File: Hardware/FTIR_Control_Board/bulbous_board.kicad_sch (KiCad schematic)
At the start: 26 parts, among them J1 RJ45_LED_Shielded, Q1 NMOS, U1 OKI, U2 Peensy4.1_DEV-16771, U3 TMC2208

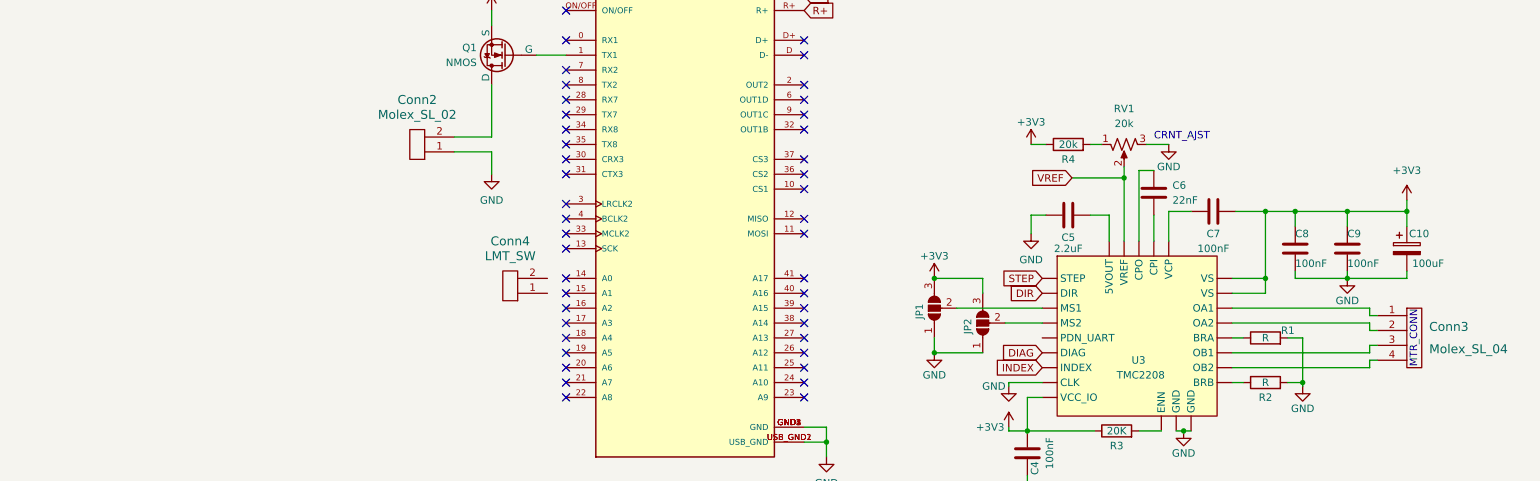
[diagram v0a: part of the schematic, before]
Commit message: Added Photodetector
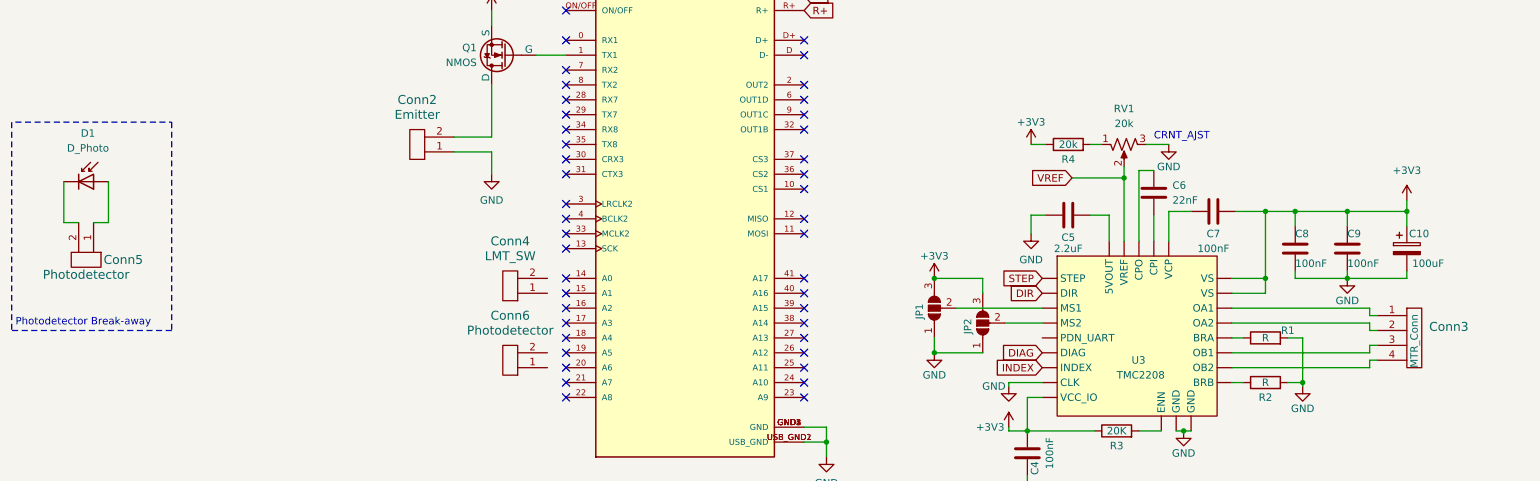
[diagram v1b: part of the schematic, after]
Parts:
- added Conn5, Conn6: Photodetector, symbol MRDT_Connectors:Molex_SL_02
- added D1: D_Photo, symbol Device:D_Photo
- Conn2: value Molex_SL_02 -> Emitter
- Conn3: value Molex_SL_04 -> MTR_Conn
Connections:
- new net: Conn5.2, D1.1 (K)
- new net: Conn5.1, D1.2 (A)
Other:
- note added: "Photodetector Break-away"
- note removed: "MTR_CONN"
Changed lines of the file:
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@@
     (stroke (width 0) (type default))
+  )
+  (polyline (pts (xy 24.13 93.345) (xy 24.13 128.905))
+    (stroke (width 0) (type dash))
   )
   (wire (pts (xy 238.125 108.585) (xy 238.125 120.015))
@@
     (stroke (width 0) (type default))
   )
+  (wire (pts (xy 38.1 110.49) (xy 40.64 110.49))
+    (stroke (width 0) (type default))
+  )
   (wire (pts (xy 163.195 147.955) (xy 163.195 150.495))
     (stroke (width 0) (type default))
@@
     (stroke (width 0) (type default))
   )
+  (wire (pts (xy 35.56 110.49) (xy 33.02 110.49))
+    (stroke (width 0) (type default))
+  )
   (wire (pts (xy 262.255 118.745) (xy 262.255 120.015))
     (stroke (width 0) (type default))
@@
     (stroke (width 0) (type default))
   )
+  (wire (pts (xy 33.02 110.49) (xy 33.02 103.505))
+    (stroke (width 0) (type default))
+  )
   (wire (pts (xy 79.375 33.02) (xy 83.185 33.02))
     (stroke (width 0) (type default))
@@
     (stroke (width 0) (type default))
   )
+  (polyline (pts (xy 51.435 93.345) (xy 51.435 128.905))
+    (stroke (width 0) (type dash))
+  )
   (wire (pts (xy 255.905 131.445) (xy 257.175 131.445))
     (stroke (width 0) (type default))
@@
     (stroke (width 0) (type default))
   )
+  (polyline (pts (xy 24.765 93.345) (xy 51.435 93.345))
+    (stroke (width 0) (type dash))
+  )
   (wire (pts (xy 271.145 53.975) (xy 274.955 53.975))
     (stroke (width 0) (type default))
@@
     (stroke (width 0) (type default))
   )
+  (wire (pts (xy 40.64 110.49) (xy 40.64 103.505))
+    (stroke (width 0) (type default))
+  )
   (wire (pts (xy 241.935 130.175) (xy 244.475 130.175))
     (stroke (width 0) (type default))
@@
   (wire (pts (xy 274.955 22.225) (xy 274.955 53.975))
     (stroke (width 0) (type default))
+  )
+  (polyline (pts (xy 51.435 128.905) (xy 24.13 128.905))
+    (stroke (width 0) (type dash))
   )
   (wire (pts (xy 193.675 127.635) (xy 200.025 127.635))
@@
     (effects (font (size 1.27 1.27)) (justify left bottom))
   )
-  (text "MTR_CONN" (at 264.16 135.255 90)
+  (text "Photodetector Break-away" (at 24.765 128.27 0)
     (effects (font (size 1.27 1.27)) (justify left bottom))
   )
@@
     )
   )
+  (symbol (lib_id "Device:D_Photo") (at 38.1 103.505 0) (unit 1)
+    (in_bom yes) (on_board yes) (dnp no) (fields_autoplaced)
+    (property "Reference" "D1" (at 37.1475 95.25 0)
+      (effects (font (size 1.27 1.27)))
+    )
+    (property "Value" "D_Photo" (at 37.1475 97.79 0)
+      (effects (font (size 1.27 1.27)))
+    )
+    (property "Footprint" "" (at 36.83 103.505 0)
+      (effects (font (size 1.27 1.27)) hide)
+    )
+    (property "Datasheet" "~" (at 36.83 103.505 0)
+      (effects (font (size 1.27 1.27)) hide)
+    )
+    (pin "1")
+    (pin "2")
+    (instances
+      (project "bulbous_board"
+        (path "/049c3f09-c046-40c3-9872-e62b40667976"
+          (reference "D1") (unit 1)
+        )
+      )
+    )
+  )
   (symbol (lib_id "MRDT_Devices:OKI") (at 64.135 35.56 0) (unit 1)
     (in_bom yes) (on_board yes) (dnp no) (fields_autoplaced)
@@
     )
   )
+  (symbol (lib_id "MRDT_Connectors:Molex_SL_02") (at 34.29 115.57 270) (unit 1)
+    (in_bom yes) (on_board yes) (dnp no)
+    (property "Reference" "Conn5" (at 43.18 116.84 90)
+      (effects (font (size 1.524 1.524)))
+    )
+    (property "Value" "Photodetector" (at 36.83 119.38 90)
+      (effects (font (size 1.524 1.524)))
+    )
+    (property "Footprint" "" (at 31.75 115.57 0)
+      (effects (font (size 1.524 1.524)) hide)
+    )
+    (property "Datasheet" "" (at 31.75 115.57 0)
+      (effects (font (size 1.524 1.524)) hide)
+    )
+    (pin "1")
+    (pin "2")
+    (instances
+      (project "bulbous_board"
+        (path "/049c3f09-c046-40c3-9872-e62b40667976"
+          (reference "Conn5") (unit 1)
+        )
+      )
+    )
+  )
   (symbol (lib_id "Device:C") (at 204.47 109.22 90) (unit 1)
     (in_bom yes) (on_board yes) (dnp no)
@@
     )
   )
+  (symbol (lib_id "MRDT_Connectors:Molex_SL_02") (at 110.49 131.445 180) (unit 1)
+    (in_bom yes) (on_board yes) (dnp no)
+    (property "Reference" "Conn6" (at 109.22 126.365 0)
+      (effects (font (size 1.524 1.524)))
+    )
+    (property "Value" "Photodetector" (at 109.22 128.905 0)
+      (effects (font (size 1.524 1.524)))
+    )
+    (property "Footprint" "" (at 110.49 128.905 0)
+      (effects (font (size 1.524 1.524)) hide)
+    )
+    (property "Datasheet" "" (at 110.49 128.905 0)
+      (effects (font (size 1.524 1.524)) hide)
+    )
+    (pin "1")
+    (pin "2")
+    (instances
+      (project "bulbous_board"
+        (path "/049c3f09-c046-40c3-9872-e62b40667976"
+          (reference "Conn6") (unit 1)
+        )
+      )
+    )
+  )
   (symbol (lib_id "MRDT_Connectors:Molex_SL_04") (at 262.255 135.255 0) (unit 1)
     (in_bom yes) (on_board yes) (dnp no)
@@
       (effects (font (size 1.524 1.524)) (justify left))
     )
-    (property "Value" "Molex_SL_04" (at 266.065 132.08 0)
-      (effects (font (size 1.524 1.524)) (justify left))
+    (property "Value" "MTR_Conn" (at 263.525 135.255 90)
+      (effects (font (size 1.27 1.27)) (justify left))
     )
     (property "Footprint" "" (at 262.255 135.255 0)
@@
       (effects (font (size 1.524 1.524)))
     )
-    (property "Value" "Molex_SL_02" (at 93.345 92.075 0)
+    (property "Value" "Emitter" (at 93.345 92.075 0)
       (effects (font (size 1.524 1.524)))
     )

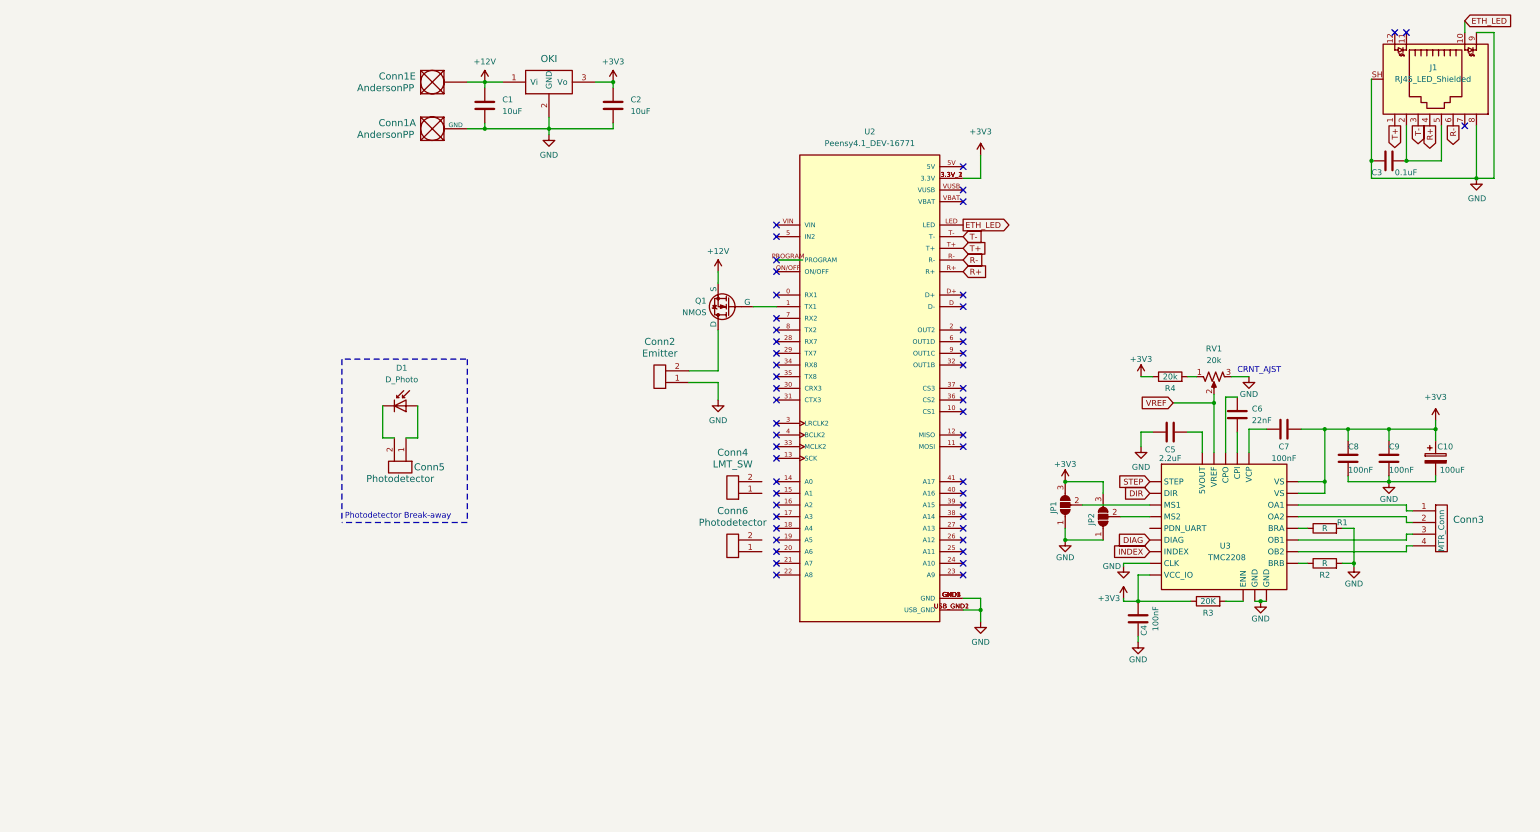
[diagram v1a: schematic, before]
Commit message: Stepper Driver Changes
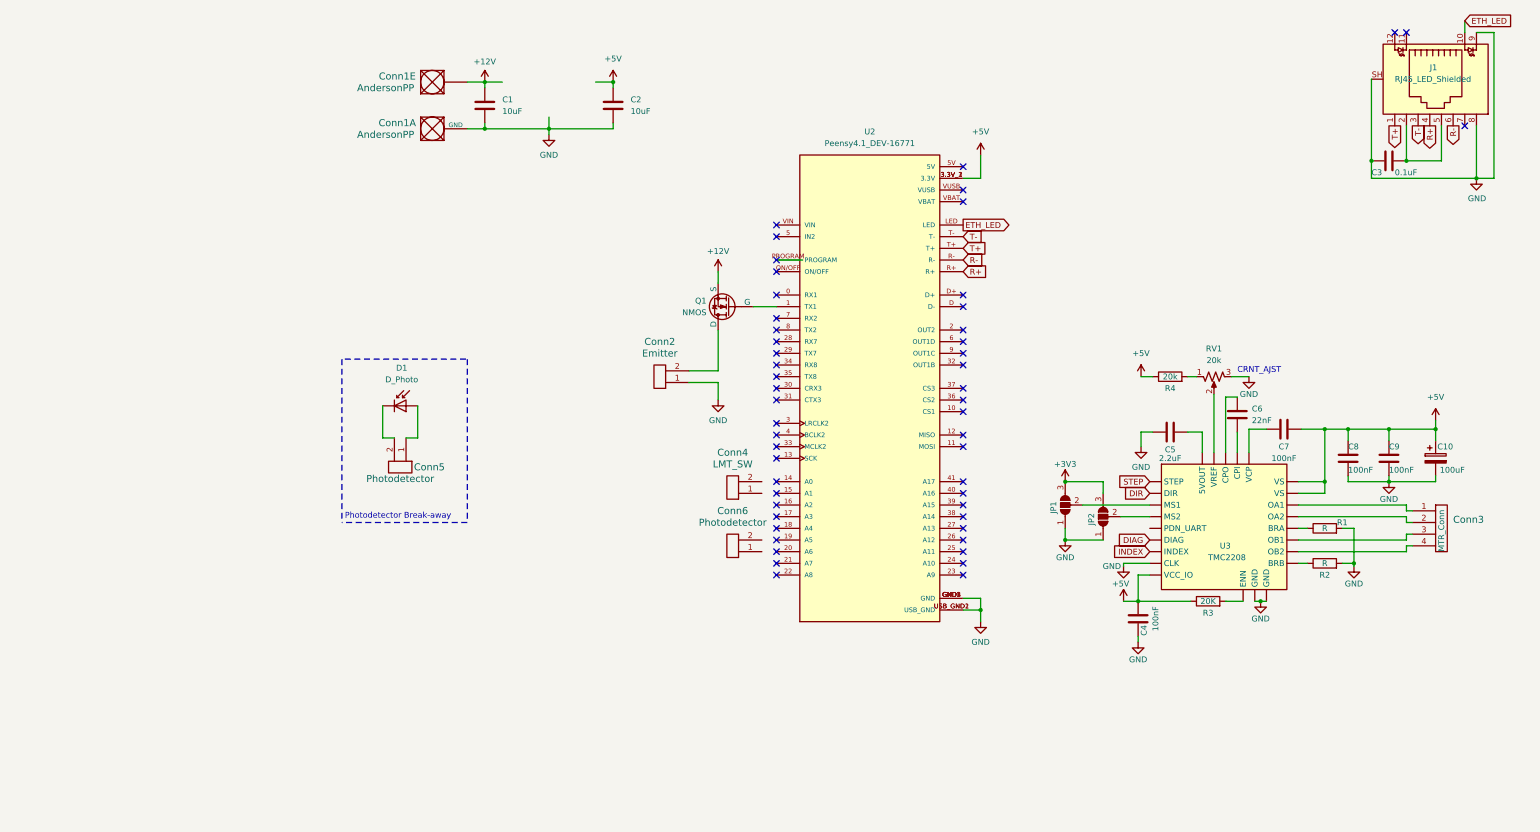
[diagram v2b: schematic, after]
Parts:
- removed U1: OKI, MRDT_Devices:OKI_Horizontal, symbol MRDT_Devices:OKI
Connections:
- net +3V3: no longer C10.1, C2.1, C4.1, C7.2, C8.1, C9.1, R3.1, R4.1, U2.3.3V_1 (3.3V), U2.3.3V_2 (3.3V), U2.3.3V_3 (3.3V), U3. (VS)
- net VREF: no longer names the net of RV1.2, U3. (VS)
- new net +5V: C10.1, C2.1, C4.1, C7.2, C8.1, C9.1, R3.1, R4.1, U2.3.3V_1 (3.3V), U2.3.3V_2 (3.3V), U2.3.3V_3 (3.3V), U3. (VS)

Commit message: Idk
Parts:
- added U1: TSR_1-2450, Converter_DCDC:Converter_DCDC_TRACO_TSR-1_THT, symbol Regulator_Switching:TSR_1-2450
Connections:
- net +3V3 is gone; now on net +5V: JP1.3 (B), JP2.3 (B)
- net +12V: now also U1.1 (Vin)
- net +5V: now also U1.3 (Vout)
- net GND: now also U1.2 (GND)
- net UART: now reaches U3. (VS)
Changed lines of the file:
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@@
   (junction (at 271.145 53.975) (diameter 0) (color 0 0 0 0)
   )
+  (junction (at 224.155 146.05) (diameter 0) (color 0 0 0 0)
+  )
   (junction (at 181.61 120.015) (diameter 0) (color 0 0 0 0)
-  )
-  (junction (at 224.155 146.05) (diameter 0) (color 0 0 0 0)
   )
   (junction (at 255.905 50.165) (diameter 0) (color 0 0 0 0)
@@
     )
   )
+  (global_label "UART" (shape input) (at 200.025 130.175 180) (fields_autoplaced)
+    (effects (font (size 1.27 1.27)) (justify right))
+    (property "Intersheetrefs" "${INTERSHEET_REFS}" (at 192.3831 130.175 0)
+      (effects (font (size 1.27 1.27)) (justify right) hide)
+    )
+  )
   (global_label "INDEX" (shape input) (at 200.025 135.255 180) (fields_autoplaced)
     (effects (font (size 1.27 1.27)) (justify right))
@@
     )
   )
+  (symbol (lib_id "Regulator_Switching:TSR_1-2450") (at 69.215 35.56 0) (unit 1)
+    (in_bom yes) (on_board yes) (dnp no) (fields_autoplaced)
+    (property "Reference" "U1" (at 69.215 25.4 0)
+      (effects (font (size 1.27 1.27)))
+    )
+    (property "Value" "TSR_1-2450" (at 69.215 27.94 0)
+      (effects (font (size 1.27 1.27)))
+    )
+    (property "Footprint" "Converter_DCDC:Converter_DCDC_TRACO_TSR-1_THT" (at 69.215 39.37 0)
+      (effects (font (size 1.27 1.27) italic) (justify left) hide)
+    )
+    (property "Datasheet" "http://www.tracopower.com/products/tsr1.pdf" (at 69.215 35.56 0)
+      (effects (font (size 1.27 1.27)) hide)
+    )
+    (pin "1")
+    (pin "2")
+    (pin "3")
+    (instances
+      (project "bulbous_board"
+        (path "/049c3f09-c046-40c3-9872-e62b40667976"
+          (reference "U1") (unit 1)
+        )
+      )
+    )
+  )
   (symbol (lib_id "power:+5V") (at 163.195 48.895 0) (unit 1)
     (in_bom yes) (on_board yes) (dnp no) (fields_autoplaced)
@@
         (path "/049c3f09-c046-40c3-9872-e62b40667976"
           (reference "Q1") (unit 1)
+        )
+      )
+    )
+  )
+  (symbol (lib_id "power:+5V") (at 181.61 120.015 0) (unit 1)
+    (in_bom yes) (on_board yes) (dnp no) (fields_autoplaced)
+    (property "Reference" "#PWR017" (at 181.61 123.825 0)
+      (effects (font (size 1.27 1.27)) hide)
+    )
+    (property "Value" "+5V" (at 181.61 114.935 0)
+      (effects (font (size 1.27 1.27)))
+    )
+    (property "Footprint" "" (at 181.61 120.015 0)
+      (effects (font (size 1.27 1.27)) hide)
+    )
+    (property "Datasheet" "" (at 181.61 120.015 0)
+      (effects (font (size 1.27 1.27)) hide)
+    )
+    (pin "1")
+    (instances
+      (project "bulbous_board"
+        (path "/049c3f09-c046-40c3-9872-e62b40667976"
+          (reference "#PWR017") (unit 1)
         )
       )
@@
         )
       )
-    )
-  )
-  (symbol (lib_id "power:+3V3") (at 181.61 120.015 0) (unit 1)
-    (in_bom yes) (on_board yes) (dnp no)
-    (property "Reference" "#PWR019" (at 181.61 123.825 0)
-      (effects (font (size 1.27 1.27)) hide)
-    )
-    (property "Value" "+3V3" (at 181.61 116.205 0)
-      (effects (font (size 1.27 1.27)))
-    )
-    (property "Footprint" "" (at 181.61 120.015 0)
-      (effects (font (size 1.27 1.27)) hide)
-    )
-    (property "Datasheet" "" (at 181.61 120.015 0)
-      (effects (font (size 1.27 1.27)) hide)
-    )
-    (pin "1")
-    (instances
-      (project "bulbous_board"
-        (path "/049c3f09-c046-40c3-9872-e62b40667976"
-          (reference "#PWR019") (unit 1)
-        )
-      )
